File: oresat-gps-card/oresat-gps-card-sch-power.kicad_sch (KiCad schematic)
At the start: 97 parts, among them Q1 DMP2240UDM, Q2 PMV45EN, Q3 DMP3050LVT-7, Q4 DMP3050LVT-7, Q5 PMV45EN, U2 MAX7310ATE, U3 MIC842LYC5, U4 MIC842LYC5, U5 MAX4211FETE, U6 LTC3624, U7 TS5A21366

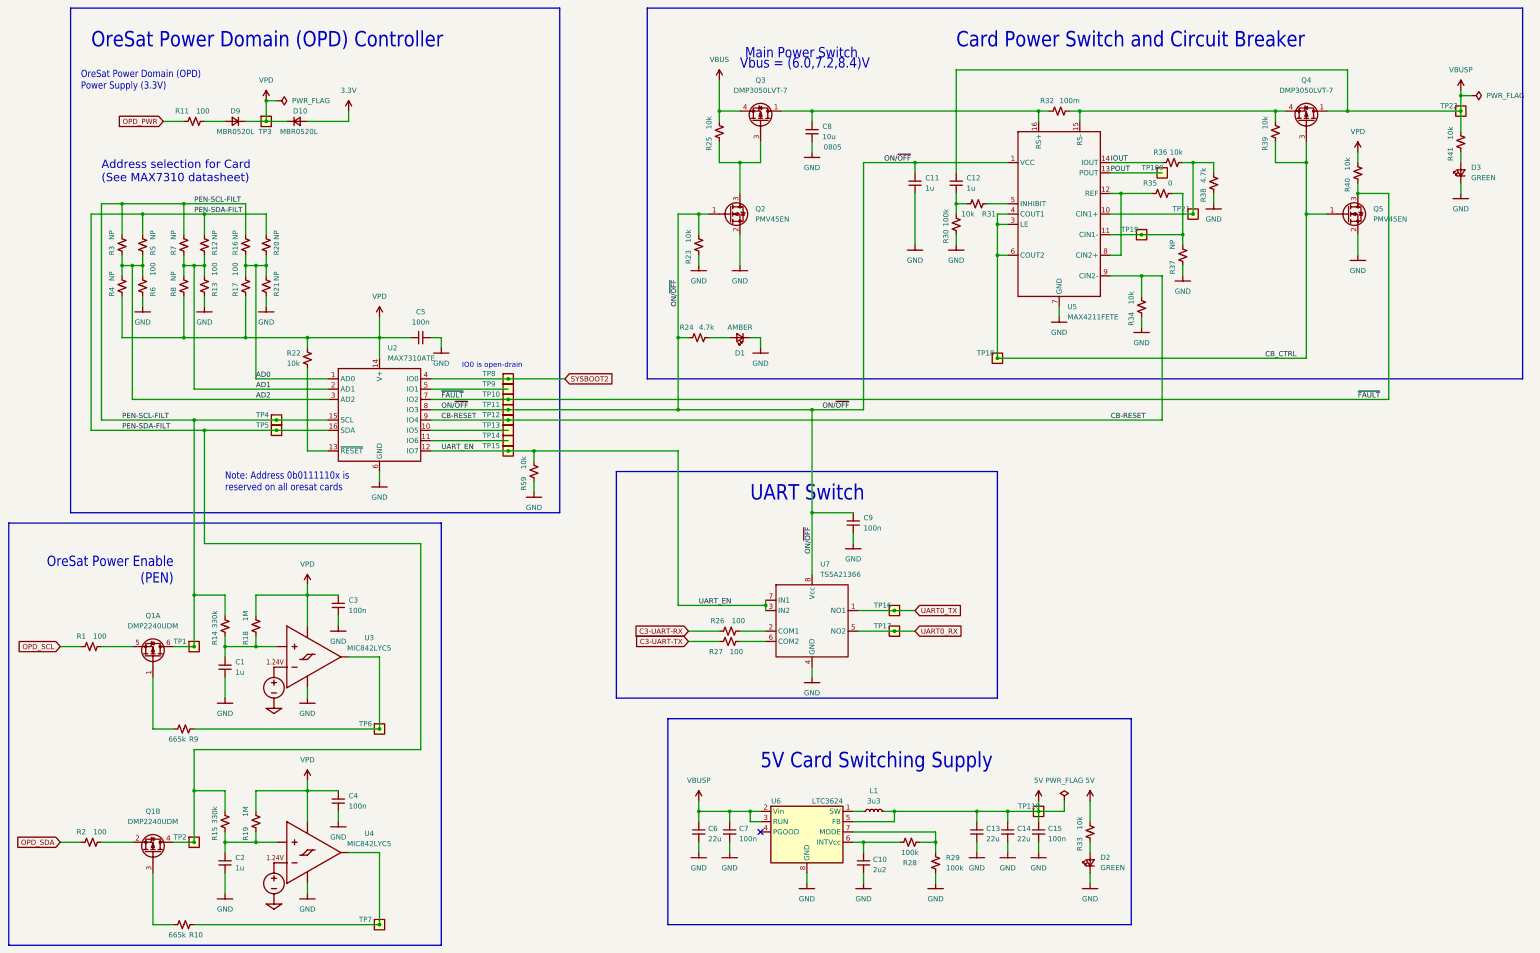
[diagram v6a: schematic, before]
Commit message: Updated KiCAD 8, updated schematic sheet info, polished some schematic things, and made DNP parts DNP.
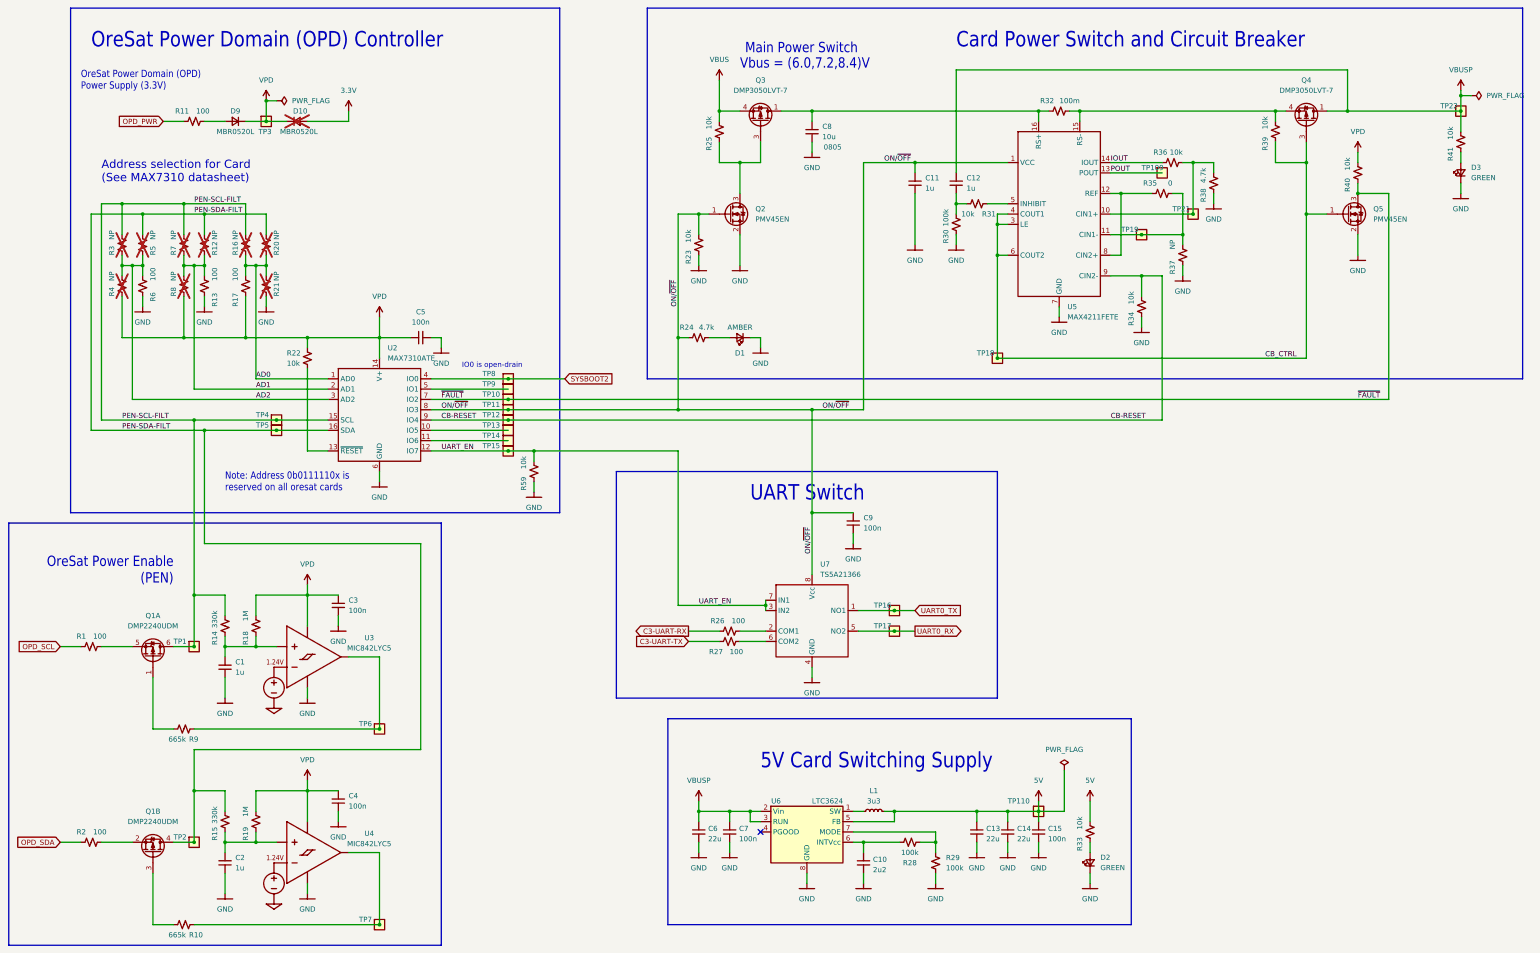
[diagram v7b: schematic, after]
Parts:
- D10, R12, R16, R20, R21, R3, R4, R5, R7, R8: now not fitted; now left out of the parts list
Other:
- title: (none) -> OreSat GPS Card

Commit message: updated symbols and started new 2771 symbol
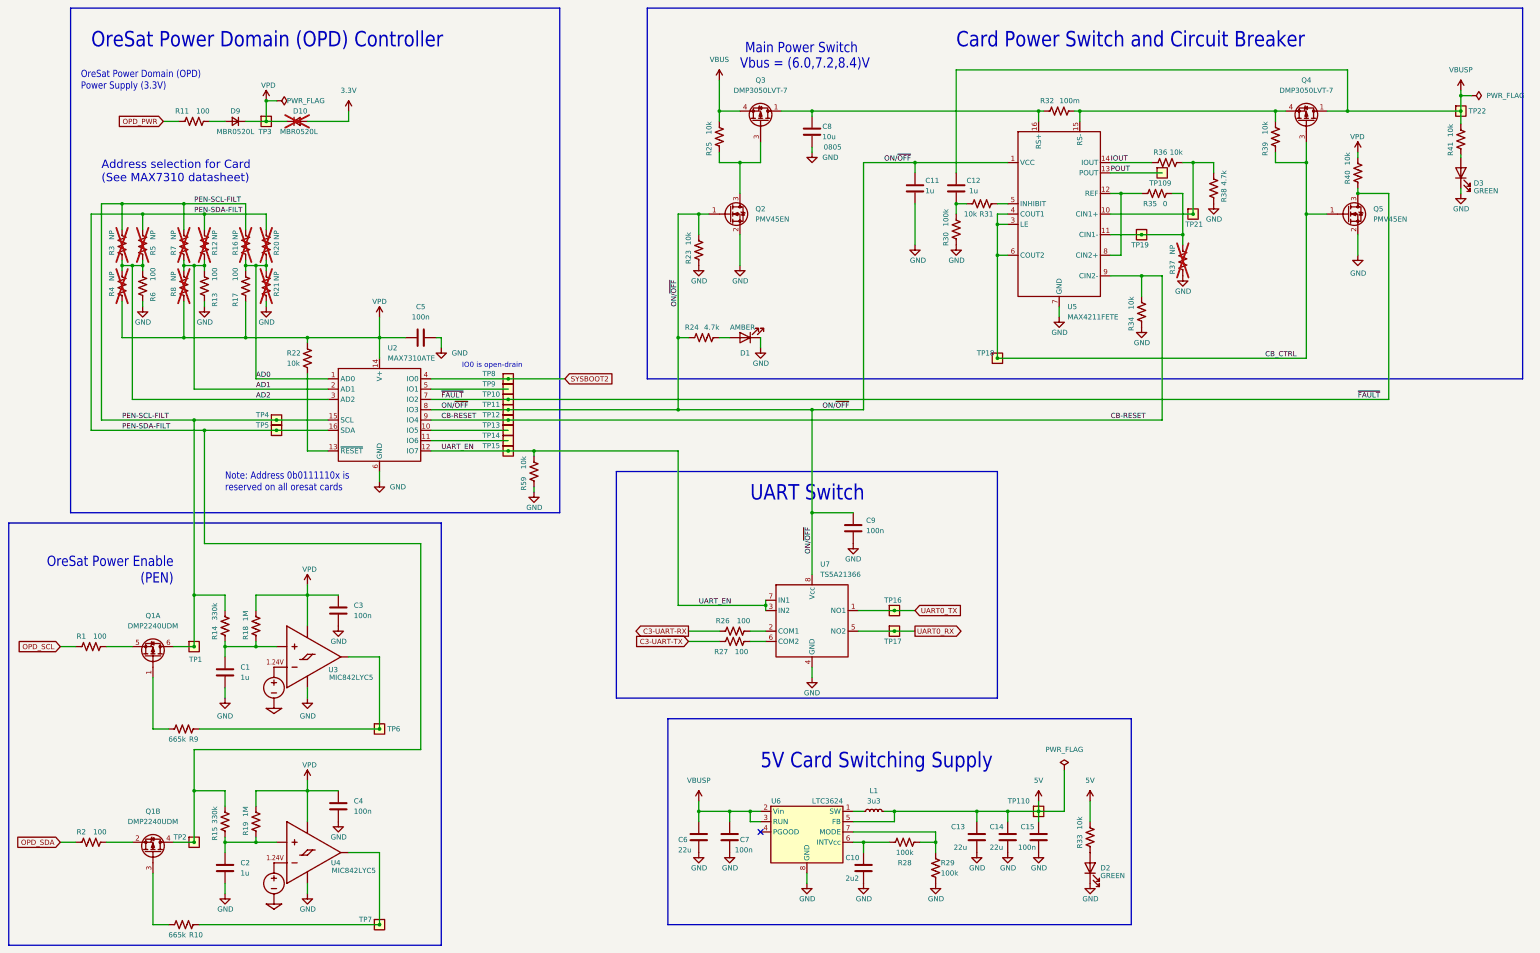
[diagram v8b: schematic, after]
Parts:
- C1, C10, C11, C12, C13, C14, C15, C2, C3, C4, C5, C6, C7, C8, C9: symbol Device:C_Small -> Device:C
- D1, D2, D3: symbol Device:LED_Small -> Device:LED
- R1, R10, R11, R13, R14, R15, R17, R18, R19, R2, R22, R23, R24, R25, R26, R27, R28, R29, R30, R31, R32, R33, R34, R35, R36, R38, R39, R40, R41, R59, R6, R9: symbol Device:R_Small_US -> Device:R_US
- R12, R16, R20, R21, R3, R4, R5, R7, R8: symbol Device:R_Small_US -> Device:R_US; now in the parts list
- R37: symbol Device:R_Small_US -> Device:R_US; now not fitted
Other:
- moved on the sheet: C1, C10, C11, C12, C13, C14, C15, C2, C3, C4, C6, C7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
